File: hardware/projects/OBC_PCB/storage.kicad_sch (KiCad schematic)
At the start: 8 parts, among them J2 DM3CS-SF

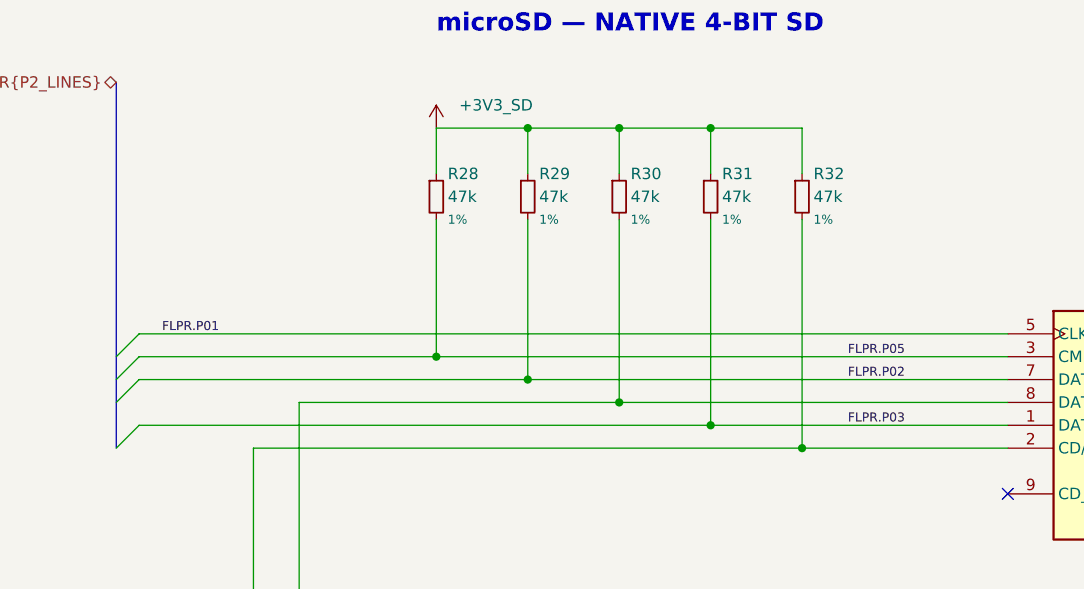
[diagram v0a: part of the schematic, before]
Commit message: fix(hardware): apply schematic review and peripheral pin mapping
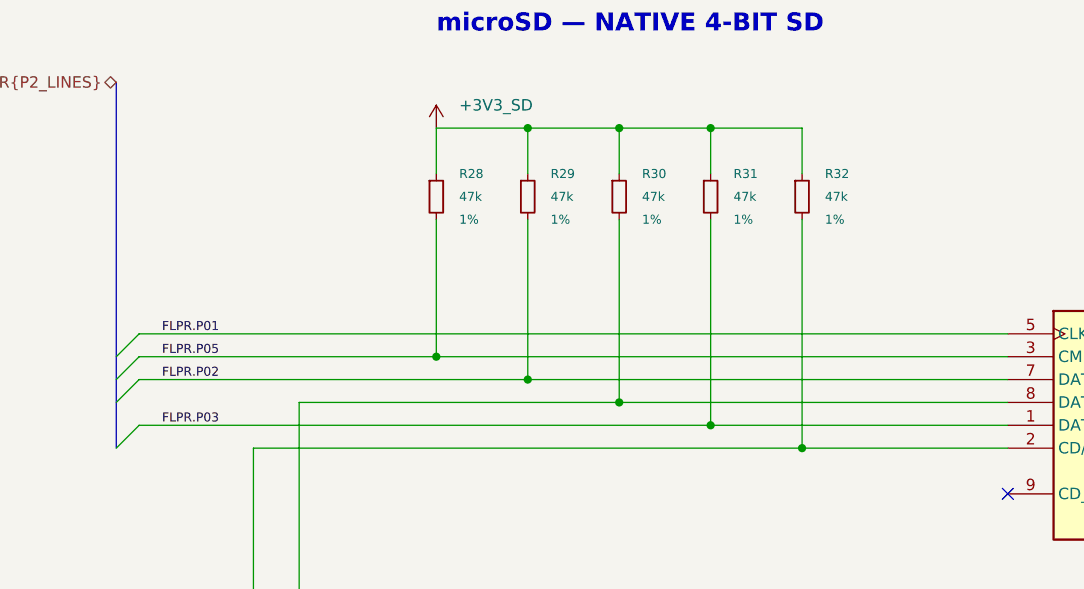
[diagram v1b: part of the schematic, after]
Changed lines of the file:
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@@
 	)
 	(label "FLPR.P05"
-		(at 137.16 83.82 0)
+		(at 60.96 83.82 0)
 		(effects
 			(font
@@
 		(fields_autoplaced yes)
 		(property "Reference" "R28"
-			(at 92.71 63.5 0)
-			(show_name no)
-			(do_not_autoplace no)
-			(effects
-				(font
-					(size 1.27 1.27)
+			(at 93.98 63.50000000000001 0)
+			(show_name no)
+			(do_not_autoplace no)
+			(effects
+				(font
+					(size 1 1)
 				)
 				(justify left)
@@
 		)
 		(property "Value" "47k"
-			(at 92.71 66.04 0)
-			(show_name no)
-			(do_not_autoplace no)
-			(effects
-				(font
-					(size 1.27 1.27)
+			(at 93.98 66.04 0)
+			(show_name no)
+			(do_not_autoplace no)
+			(effects
+				(font
+					(size 1 1)
 				)
 				(justify left)
@@
 		)
 		(property "Tolerance" "1%"
-			(at 92.71 68.58 0)
+			(at 93.98 68.58000000000001 0)
 			(effects
 				(font
@@
 	)
 	(label "FLPR.P02"
-		(at 137.16 86.36 0)
+		(at 60.96 86.36 0)
 		(effects
 			(font
@@
 		(fields_autoplaced yes)
 		(property "Reference" "R29"
-			(at 102.87 63.5 0)
-			(show_name no)
-			(do_not_autoplace no)
-			(effects
-				(font
-					(size 1.27 1.27)
+			(at 104.14 63.50000000000001 0)
+			(show_name no)
+			(do_not_autoplace no)
+			(effects
+				(font
+					(size 1 1)
 				)
 				(justify left)
@@
 		)
 		(property "Value" "47k"
-			(at 102.87 66.04 0)
-			(show_name no)
-			(do_not_autoplace no)
-			(effects
-				(font
-					(size 1.27 1.27)
+			(at 104.14 66.04 0)
+			(show_name no)
+			(do_not_autoplace no)
+			(effects
+				(font
+					(size 1 1)
 				)
 				(justify left)
@@
 		)
 		(property "Tolerance" "1%"
-			(at 102.87 68.58 0)
+			(at 104.14 68.58000000000001 0)
 			(effects
 				(font
@@
 		(fields_autoplaced yes)
 		(property "Reference" "R30"
-			(at 113.03 63.5 0)
-			(show_name no)
-			(do_not_autoplace no)
-			(effects
-				(font
-					(size 1.27 1.27)
+			(at 114.30000000000001 63.50000000000001 0)
+			(show_name no)
+			(do_not_autoplace no)
+			(effects
+				(font
+					(size 1 1)
 				)
 				(justify left)
@@
 		)
 		(property "Value" "47k"
-			(at 113.03 66.04 0)
-			(show_name no)
-			(do_not_autoplace no)
-			(effects
-				(font
-					(size 1.27 1.27)
+			(at 114.30000000000001 66.04 0)
+			(show_name no)
+			(do_not_autoplace no)
+			(effects
+				(font
+					(size 1 1)
 				)
 				(justify left)
@@
 		)
 		(property "Tolerance" "1%"
-			(at 113.03 68.58 0)
+			(at 114.30000000000001 68.58000000000001 0)
 			(effects
 				(font
@@
 	)
 	(label "FLPR.P03"
-		(at 137.16 91.44 0)
+		(at 60.96 91.44 0)
 		(effects
 			(font
@@
 		(fields_autoplaced yes)
 		(property "Reference" "R31"
-			(at 123.19 63.5 0)
-			(show_name no)
-			(do_not_autoplace no)
-			(effects
-				(font
-					(size 1.27 1.27)
+			(at 124.46000000000001 63.50000000000001 0)
+			(show_name no)
+			(do_not_autoplace no)
+			(effects
+				(font
+					(size 1 1)
 				)
 				(justify left)
@@
 		)
 		(property "Value" "47k"
-			(at 123.19 66.04 0)
-			(show_name no)
-			(do_not_autoplace no)
-			(effects
-				(font
-					(size 1.27 1.27)
+			(at 124.46000000000001 66.04 0)
+			(show_name no)
+			(do_not_autoplace no)
+			(effects
+				(font
+					(size 1 1)
 				)
 				(justify left)
@@
 		)
 		(property "Tolerance" "1%"
-			(at 123.19 68.58 0)
+			(at 124.46000000000001 68.58000000000001 0)
 			(effects
 				(font
@@
 		(fields_autoplaced yes)
 		(property "Reference" "R32"
-			(at 133.35 63.5 0)
-			(show_name no)
-			(do_not_autoplace no)
-			(effects
-				(font
-					(size 1.27 1.27)
+			(at 134.62 63.50000000000001 0)
+			(show_name no)
+			(do_not_autoplace no)
+			(effects
+				(font
+					(size 1 1)
 				)
 				(justify left)
@@
 		)
 		(property "Value" "47k"
-			(at 133.35 66.04 0)
-			(show_name no)
-			(do_not_autoplace no)
-			(effects
-				(font
-					(size 1.27 1.27)
+			(at 134.62 66.04 0)
+			(show_name no)
+			(do_not_autoplace no)
+			(effects
+				(font
+					(size 1 1)
 				)
 				(justify left)
@@
 		)
 		(property "Tolerance" "1%"
-			(at 133.35 68.58 0)
-			(effects
-				(font
+			(at 134.62 68.58000000000001 0)
+			(effects
+				(font

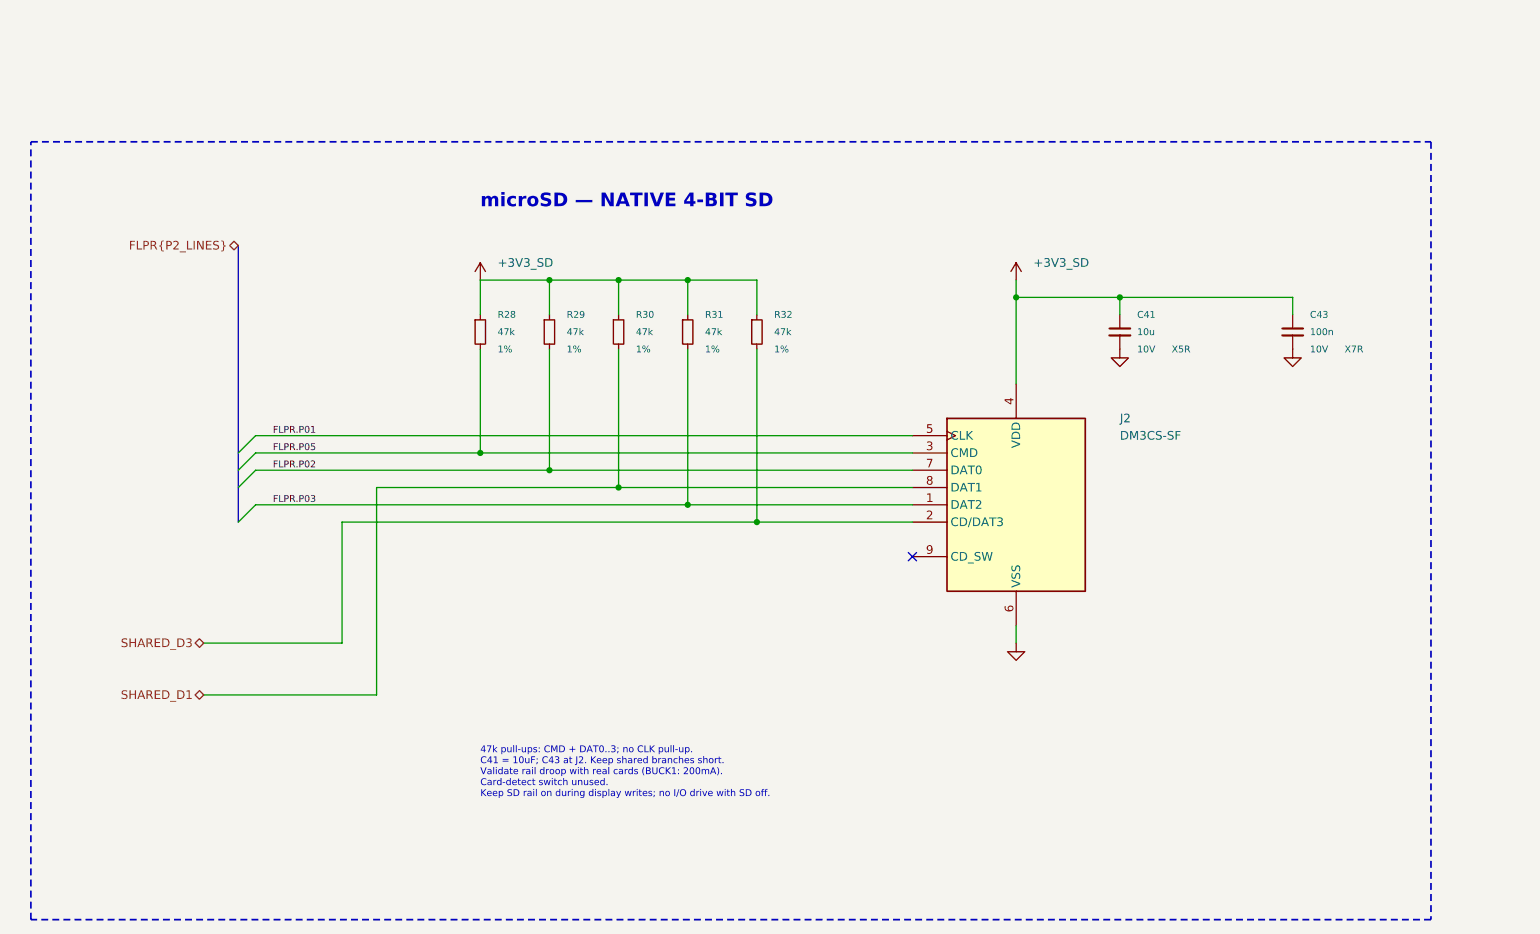
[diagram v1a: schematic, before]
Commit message: hardware: prepare QFN schematic for non-HDI boards
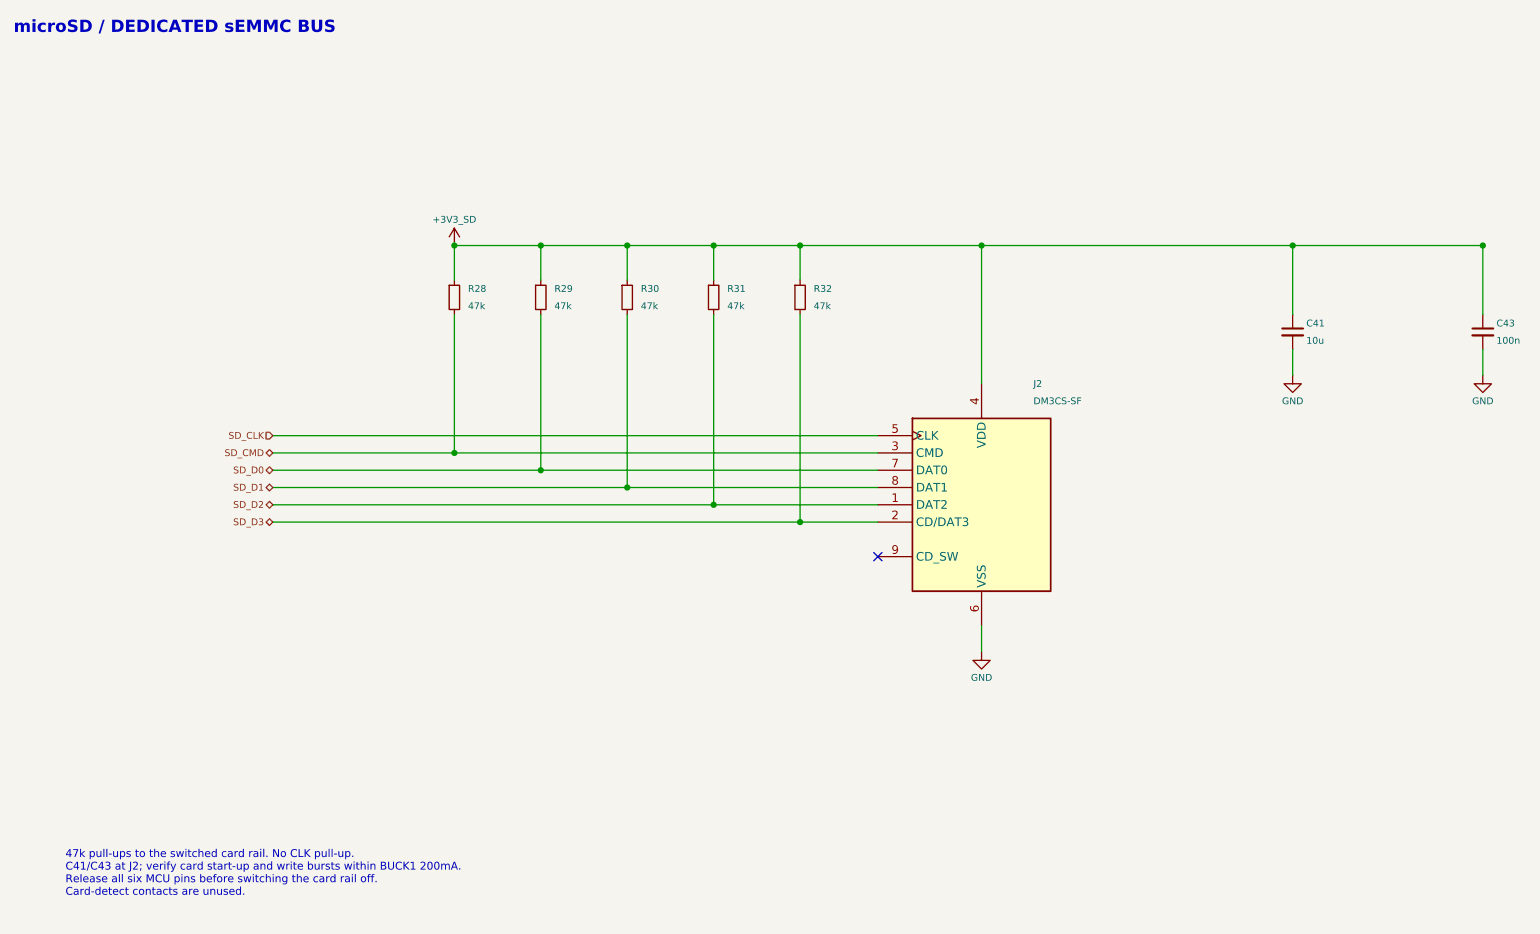
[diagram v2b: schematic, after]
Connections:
- net FLPR.P01 renamed SD_CLK
- net FLPR.P02 renamed SD_D0
- net FLPR.P03 renamed SD_D2
- net FLPR.P05 renamed SD_CMD
- net SHARED_D1 renamed SD_D1
- net SHARED_D3 renamed SD_D3
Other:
- note added: "47k pull-ups to the switched card rail. No CLK pull-up. C41/C43 at J2; verify card start-up and write bursts within BUCK1 200mA. Release all six MCU pins before switching the card rail off. Card-detect contacts are unused."
- note added: "microSD / DEDICATED sEMMC BUS"
- note removed: "47k pull-ups: CMD + DAT0..3; no CLK pull-up. C41 = 10uF; C43 at J2. Keep shared branches short. Validate rail droop with real cards (BUCK1: 200mA). Card-detect switch unused. Keep SD rail on during display writes; no I/O drive with SD off."
- note removed: "microSD — NATIVE 4-BIT SD"
- title: OpenBikeComputer — Storage -> OpenBikeComputer - microSD
- moved on the sheet: C41, C43, J2, R28, R29, R30, R31, R32
